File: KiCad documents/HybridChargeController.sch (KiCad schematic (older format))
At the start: 99 parts, among them P1 Load, P2 LI_balancer, P3 PV, P4 Extra, P5 LI, P6 LA, Q1 MMBT3904, Q10 MMBT3904, Q11 IPD90P04P4L-04, Q12 STL60P4LLF6, Q13 STL60P4LLF6, Q14 IPD90P04P4L-04, Q15 BSS138, Q16 BSS138, Q2 IPD90P04P4L-04, Q3 MMBT3904, Q4 IPD90P04P4L-04, Q5 IPD90P04P4L-04, Q6 MMBT3904, Q7 MMBT3904, Q8 MMBT3904, Q9 IPD90P04P4L-04, U1 LM358D, U2 bq76920, U3 cd4051, U4 LM358D, U5 LM358D

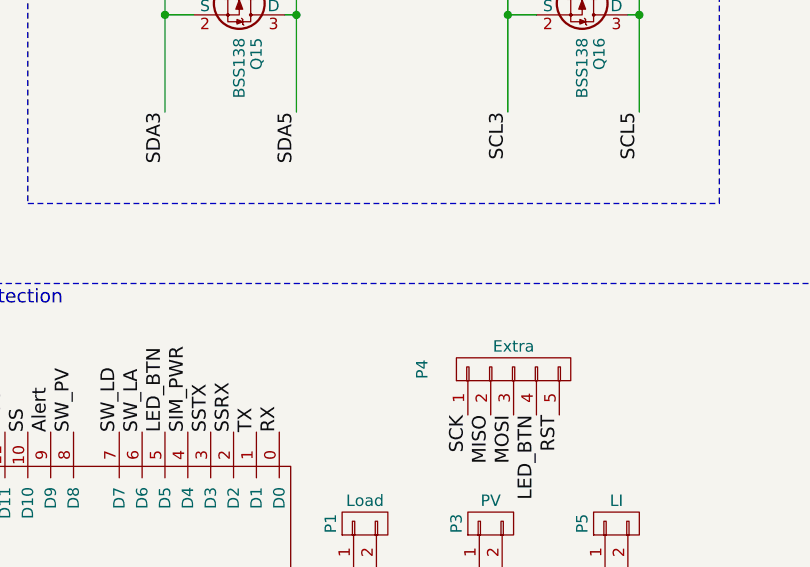
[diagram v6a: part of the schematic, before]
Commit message: added a few comments for final check, played with the Silkscreen a bit
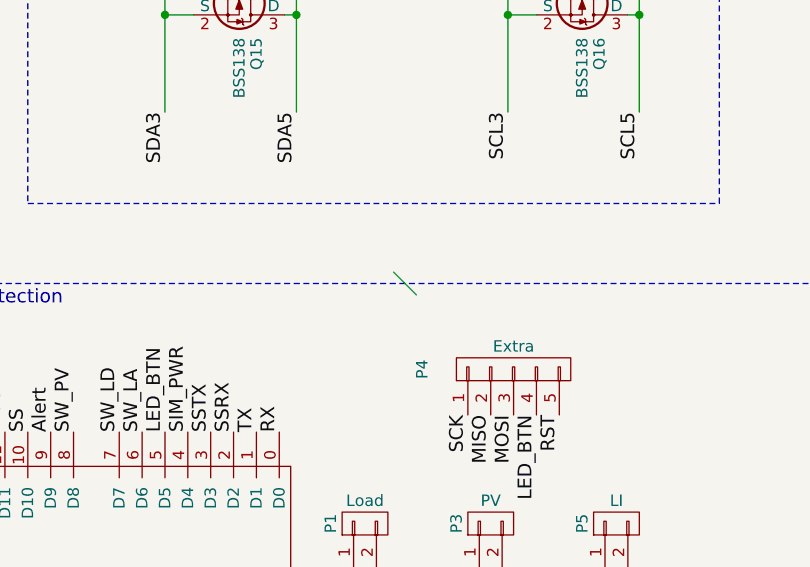
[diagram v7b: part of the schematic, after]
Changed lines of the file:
@@
 Wire Notes Line
 	11675 4100 8650 4100
+Entry Wire Line
+	10250 6200 10350 6300
 $EndSCHEMATC

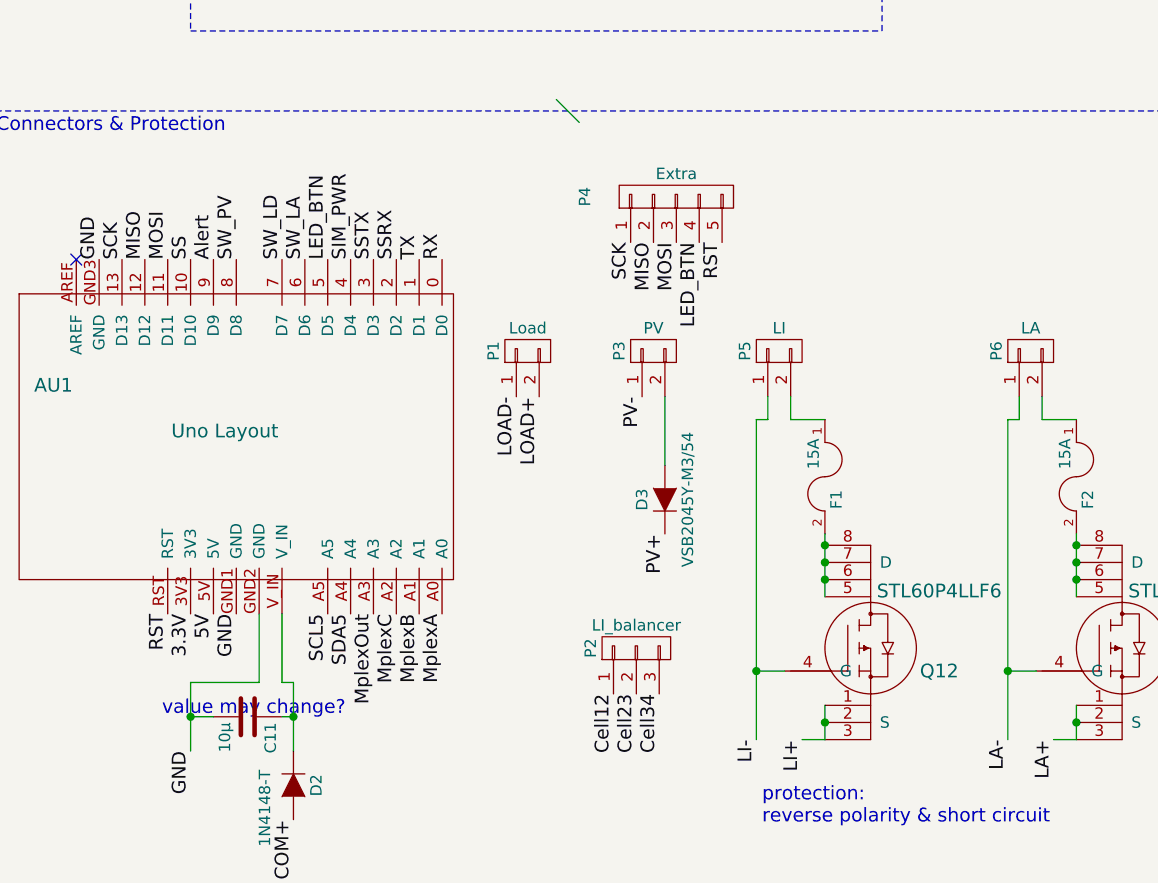
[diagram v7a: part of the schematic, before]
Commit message: added FTDI connector
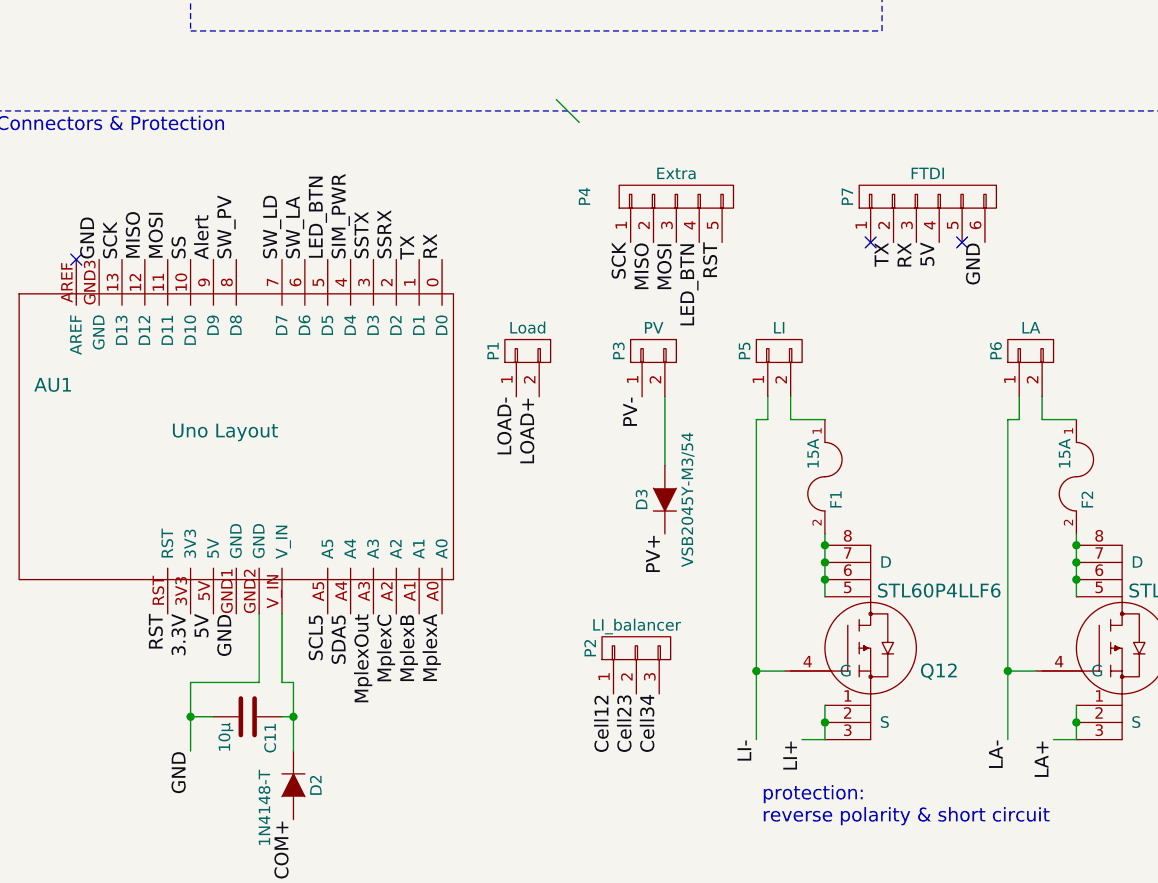
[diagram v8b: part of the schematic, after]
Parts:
- added P7: FTDI, Pin_Headers:Pin_Header_Straight_1x06_Pitch2.54mm, symbol CONN_01X06
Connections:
- net 5V: now also P7.4 (P4)
- net GND: now also P7.6 (P6)
- net RX: now also P7.3 (P3)
- net TX: now also P7.2 (P2)
- no-connect marks 5 -> 7
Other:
- note removed: "value may change?"
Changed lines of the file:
@@
 	1    0    0    -1
 $EndComp
-Text Notes 8525 8900 0    60   ~ 0
-value may change?
 Text Notes 2425 8575 0    60   ~ 0
 short!
@@
 Entry Wire Line
 	10250 6200 10350 6300
+$Comp
+L CONN_01X06 P7
+U 1 1 5922E01F
+P 11875 6625
+F 0 "P7" H 11875 6975 50  0000 C CNN
+F 1 "FTDI" V 11975 6625 50  0000 C CNN
+F 2 "Pin_Headers:Pin_Header_Straight_1x06_Pitch2.54mm" H 11875 6625 50  0001 C CNN
+F 3 "" H 11875 6625 50  0000 C CNN
+	1    11875 6625
+	0    -1   -1   0
+$EndComp
+NoConn ~ 11625 6825
+NoConn ~ 12025 6825
+Text Label 11725 6825 3    60   ~ 0
+TX
+Text Label 11825 6825 3    60   ~ 0
+RX
+Text Label 11925 6825 3    60   ~ 0
+5V
+Text Label 12125 6825 3    60   ~ 0
+GND
 $EndSCHEMATC
